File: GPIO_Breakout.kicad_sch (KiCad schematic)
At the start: 3 parts, among them J10 Port C/D breakout, J8 Port A breakout, J9 Port B breakout

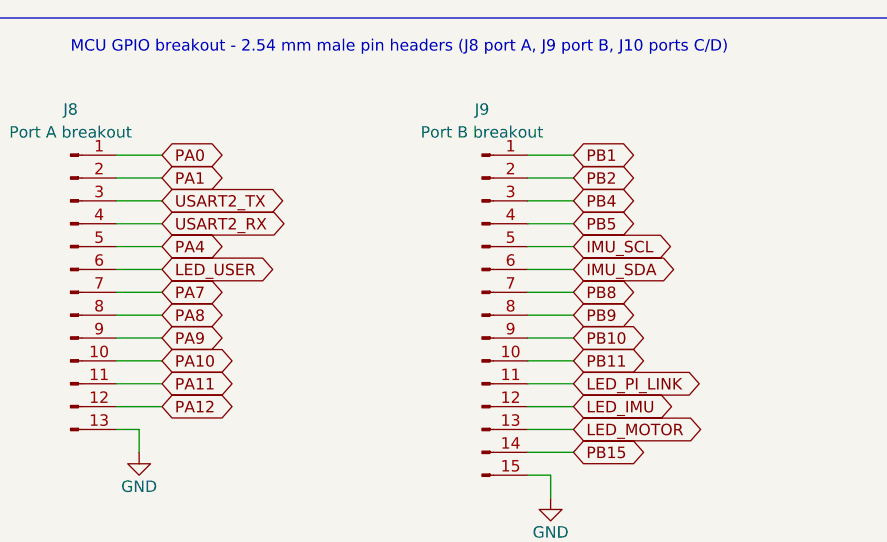
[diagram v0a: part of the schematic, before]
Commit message: Add motor 2 channel and move motor I/O to a Motor Control sheet
New Motor_Control.kicad_sch sheet (page 9) holds both channels of the
Cytron MDD20A driver and both 37D encoder connectors:
- Motor 1, moved unchanged: J6 (PWM1/DIR1/GND) and J7 (+5V 2A, A, B,
  GND)
- Motor 2, new: J16 (PWM2/DIR2/GND, Phoenix 1715035 like J6) and J15
  (encoder, same as J7)

STM32 pins:
  MOTOR1_PWM PA6 TIM3_CH1, MOTOR1_DIR PB0, ENC1_A/B PA15/PB3 (TIM2)
  MOTOR2_PWM PA7 TIM3_CH2, MOTOR2_DIR PB2, ENC2_A/B PA8/PA9 (TIM1)
Both PWMs share TIM3 (same frequency, <= 20 kHz for the MDD20A); each
encoder has its own timer in encoder mode.

The pins are shown in three places: 8 sheet pins on the root block
plus a summary note under it, a full pin and timer table inside the
sheet, and the connector descriptions. PA7/PB2/PA8/PA9 global labels
are renamed at U1 and on the J8/J9 breakout headers.

Motor 1 connectivity is unchanged; apart from J15/J16 the netlist is
identical.
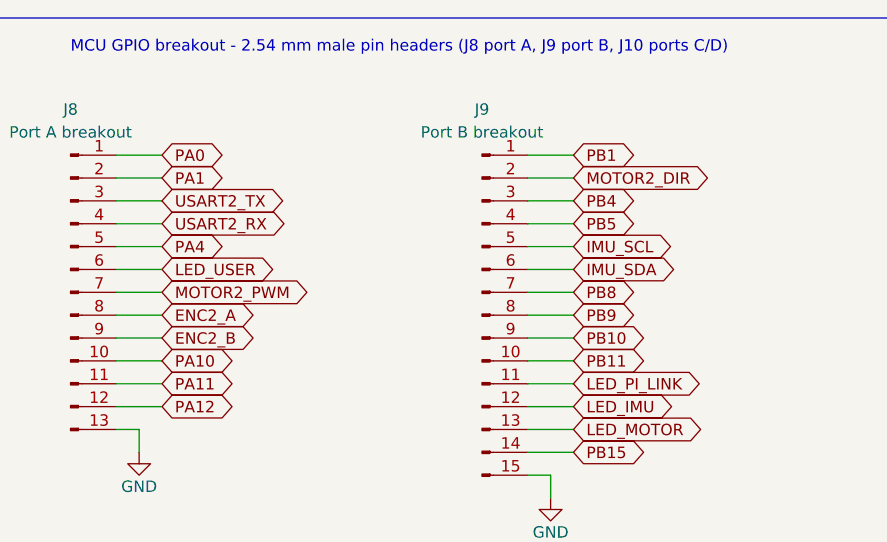
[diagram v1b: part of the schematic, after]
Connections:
- net PA7 renamed MOTOR2_PWM
- net PA8 renamed ENC2_A
- net PA9 renamed ENC2_B
- net PB2 renamed MOTOR2_DIR
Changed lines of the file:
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@@
 		)
 	)
-	(global_label "PB2"
+	(global_label "MOTOR2_DIR"
 		(shape bidirectional)
 		(at 111.76 63.5 0)
@@
 		)
 	)
-	(global_label "PA9"
+	(global_label "ENC2_B"
 		(shape bidirectional)
 		(at 66.04 81.28 0)
@@
 		)
 	)
-	(global_label "PA8"
+	(global_label "ENC2_A"
 		(shape bidirectional)
 		(at 66.04 78.74 0)
@@
 		)
 	)
-	(global_label "PA7"
+	(global_label "MOTOR2_PWM"
 		(shape bidirectional)
 		(at 66.04 76.2 0)
@@
 			)
 		)
-		(property "Description" "Male 2.54 mm pin header, 1x13 vertical: pins 1-12 = PA0, PA1, USART2_TX, USART2_RX, PA4, LED_USER, PA7, PA8, PA9, PA10, PA11, PA12; pin 13 = GND"
+		(property "Description" "Male 2.54 mm pin header, 1x13 vertical: pins 1-12 = PA0, PA1, USART2_TX, USART2_RX, PA4, LED_USER, MOTOR2_PWM (PA7), ENC2_A (PA8), ENC2_B (PA9), PA10, PA11, PA12; pin 13 = GND"
 			(at 55.88 76.2 0)
 			(hide yes)
@@
 			)
 		)
-		(property "Description" "Male 2.54 mm pin header, 1x15 vertical: pins 1-14 = PB1, PB2, PB4, PB5, IMU_SCL (PB6), IMU_SDA (PB7), PB8, PB9, PB10, PB11, LED_PI_LINK (PB12), LED_IMU (PB13), LED_MOTOR (PB14), PB15; pin 15 = GND"
+		(property "Description" "Male 2.54 mm pin header, 1x15 vertical: pins 1-14 = PB1, MOTOR2_DIR (PB2), PB4, PB5, IMU_SCL (PB6), IMU_SDA (PB7), PB8, PB9, PB10, PB11, LED_PI_LINK (PB12), LED_IMU (PB13), LED_MOTOR (PB14), PB15; pin 15 = GND"
 			(at 101.6 78.74 0)
 			(hide yes)
